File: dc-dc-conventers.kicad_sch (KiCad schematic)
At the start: 114 parts, among them Q13 DTC014TEBTL, Q14 DTC014TEBTL, Q15 DTC014TEBTL, Q18 DTC014TEBTL, U47 RT6236AHGQUF, U48 RT6236AHGQUF, U49 AP62301WU-7, U50 AP62301WU-7, U51 AP62301WU-7, U52 AP62301WU-7, U53 AP62301WU-7, U54 AP62301WU-7, U55 AP62301WU-7

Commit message: Added cosmetic changes to schematics (e.g. position of labels, designators)
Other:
- moved on the sheet: C184, C185, C186, C187, C188, C189, C190, C191, C192, C193, C194, C195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

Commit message: Fixed footprints
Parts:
- U47, U48: footprint kria-k26-devboard-footprints:RICHTEK_13-UFQFN -> antmicro-footprints:RT6236A
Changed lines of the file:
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@@
     (property "Reference" "U47" (id 0) (at 68.707 27.559 0))
     (property "Value" "RT6236AHGQUF" (id 1) (at 68.707 29.8704 0))
-    (property "Footprint" "kria-k26-devboard-footprints:RICHTEK_13-UFQFN" (id 2) (at 59.182 59.69 0)
+    (property "Footprint" "antmicro-footprints:RT6236A" (id 2) (at 59.182 59.69 0)
       (effects (font (size 1.27 1.27)) hide)
     )
@@
     (pin "2")
   )
-  (symbol (lib_id "kria-k26-devboard:RT6236AHGQUF") (at 68.834 100.838 0) (unit 1)
+  (symbol (lib_name "RT6236AHGQUF_1") (lib_id "kria-k26-devboard:RT6236AHGQUF") (at 68.834 100.838 0) (unit 1)
     (in_bom yes) (on_board yes)
     (property "Reference" "U48" (id 0) (at 68.199 81.407 0))
     (property "Value" "RT6236AHGQUF" (id 1) (at 68.199 83.7184 0))
-    (property "Footprint" "kria-k26-devboard-footprints:RICHTEK_13-UFQFN" (id 2) (at 58.674 113.538 0)
-      (effects (font (size 1.27 1.27)) hide)
-    )
+    (property "Footprint" "antmicro-footprints:RT6236A" (id 2) (at 58.674 113.538 0)
+      (effects (font (size 1.27 1.27)) hide)
+    )

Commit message: loclib
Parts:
- U47, U48: footprint antmicro-footprints:RT6236A -> kria-k26-devboard-footprints:RT6236A
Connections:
- net DC_MAIN_BUS: no longer U48.10 (VIN), U48.9 (VIN)
- net GND: no longer U48.1 (GND), U48.13 (GND)
- net SW_SOM_5V: no longer U48.12 (SW)
- net at C188.1: no longer U48.6 (PVCC)
- net at C190.1: no longer U48.5 (SS)
- net at C192.2: no longer U48.11 (BOOT)
- net at C194.1, R124.2, R125.1: no longer U48.3 (FB)
- net at R119.1: no longer U48.2 (EN)

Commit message: Replace 5V DC-DCs output capacitors to 16V rated ones
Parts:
- removed C195, C196, C197, C198, C199, C200: C_22u_0603, kria-k26-devboard-footprints:0603-cap, symbol kria-k26-devboard:C_22u_0603
- removed U48: RT6236AHGQUF, kria-k26-devboard-footprints:RT6236A, symbol kria-k26-devboard:RT6236AHGQUF
- added C195, C196, C197, C198, C199, C200: C_22u_0603_16V, antmicro-footprints:0603-cap, symbol antmicroCapacitors0603:C_22u_0603_16V
- added R156, R157, R158, R159, R160, R161, R162, R163, R164: R_0R_0603_HPWR, antmicro-footprints:0603-res, symbol antmicroResistors0603:R_0R_0603_HPWR
- added U48: RT6236AHGQUF, antmicro-footprints:RICHTEK_13-UFQFN, symbol antmicroPMICVoltageRegulatorsDCDCSwitchingRegulators:RT6236AHGQUF
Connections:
- net DC_MAIN_BUS: now also U48.10 (VIN), U48.9 (VIN); no longer C183.1, C185.1, R118.2, U47.10 (VIN), U47.9 (VIN)
- net GND: now also C196.2, C198.2, C200.2, U48.1 (GND), U48.13 (GND); no longer C183.2, C185.2, C187.2, C189.2, R123.2, U47.1 (GND), U47.13 (GND)
- net SOM_5V0: now also C196.1, C198.1, C200.1
- net SW_SOM_5V: now also U48.12 (SW)
- net USB_5V: now also C195.1, C197.1, C199.1
- net at C188.1: now also U48.6 (PVCC)
- net at C190.1: now also U48.5 (SS)
- net at C192.2: now also U48.11 (BOOT)
- net at C194.1, R124.2, R125.1: now also U48.3 (FB)
- net at R119.1: now also U48.2 (EN)
- new net: C183.2, C185.2, C187.2, C189.2, C195.2, C197.2, C199.2, R123.2, U47.1 (GND), U47.13 (GND)
- new net: C183.1, C185.1, R118.2, U47.10 (VIN), U47.9 (VIN)
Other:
- moved on the sheet: C183, C184, C185, C186, C187, C188, C189, C190, C191, C192, C193, C194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

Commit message: Add 0Ohm DC-DC output resistor WiP
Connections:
- net DC_MAIN_BUS: now also C183.1, C185.1, R118.2, U47.10 (VIN), U47.9 (VIN)
- net PL_1V2: now also R159.2; no longer C224.2, C226.2, L9.2 (P), R146.1, TP42.1
- net PL_3V3: now also R158.2; no longer C223.2, C225.2, L8.2 (P), R144.1, TP41.1
- net PS_1V0: now also R157.2; no longer C215.2, L7.2 (P), R139.1, TP40.1
- net PS_1V2: now also R156.2; no longer C214.2, C218.2, L6.2 (P), R137.1, TP39.1
- net PS_1V8: now also R164.2; no longer C213.2, C217.2, L5.2 (P), R135.1, TP38.1
- net PS_2V5: now also R163.2; no longer C212.2, L4.2 (P), R133.1, TP37.1
- net PS_3V3: now also R162.2; no longer C211.2, C216.2, L3.2 (P), R131.1, TP36.1
- net SOM_5V0: now also R161.2; no longer C194.2, C196.1, C198.1, C200.1, L2.2 (P), R124.1, TP50.1
- net USB_5V: now also R160.2; no longer C193.2, C195.1, C197.1, C199.1, L1.2 (P), R122.1, TP51.1
- net PS_1V2_OUT: now reaches R156.1
- net PS_1V2_OUT: now also C214.2, C218.2, L6.2 (P), R137.1, TP39.1
- net PS_1V8_OUT: now reaches R164.1
- net PS_1V8_OUT: now also C213.2, C217.2, L5.2 (P), R135.1, TP38.1
- net PS_3V3_OUT: now reaches R162.1
- net PS_3V3_OUT: now also C211.2, C216.2, L3.2 (P), R131.1, TP36.1
- net PS_1V0_OUT: now reaches R157.1
- net PS_1V0_OUT: now also C215.2, L7.2 (P), R139.1, TP40.1
- net PS_2V5_OUT: now reaches R163.1
- net PS_2V5_OUT: now also C212.2, L4.2 (P), R133.1, TP37.1
- net USB_5V_OUT: now reaches R160.1
- net USB_5V_OUT: now also C193.2, C195.1, C197.1, C199.1, L1.2 (P), R122.1, TP51.1
- net PL_3V3_OUT: now reaches R158.1
- net PL_3V3_OUT: now also C223.2, C225.2, L8.2 (P), R144.1, TP41.1
- net PL_1V2_OUT: now reaches R159.1
- net PL_1V2_OUT: now also C224.2, C226.2, L9.2 (P), R146.1, TP42.1
- net SOM_5V_OUT: now reaches R161.1
- net SOM_5V_OUT: now also C194.2, C196.1, C198.1, C200.1, L2.2 (P), R124.1, TP50.1
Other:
- moved on the sheet: C201, C202, C203, C204, C205, C206, C207, C208, C209, C210, C211, C212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

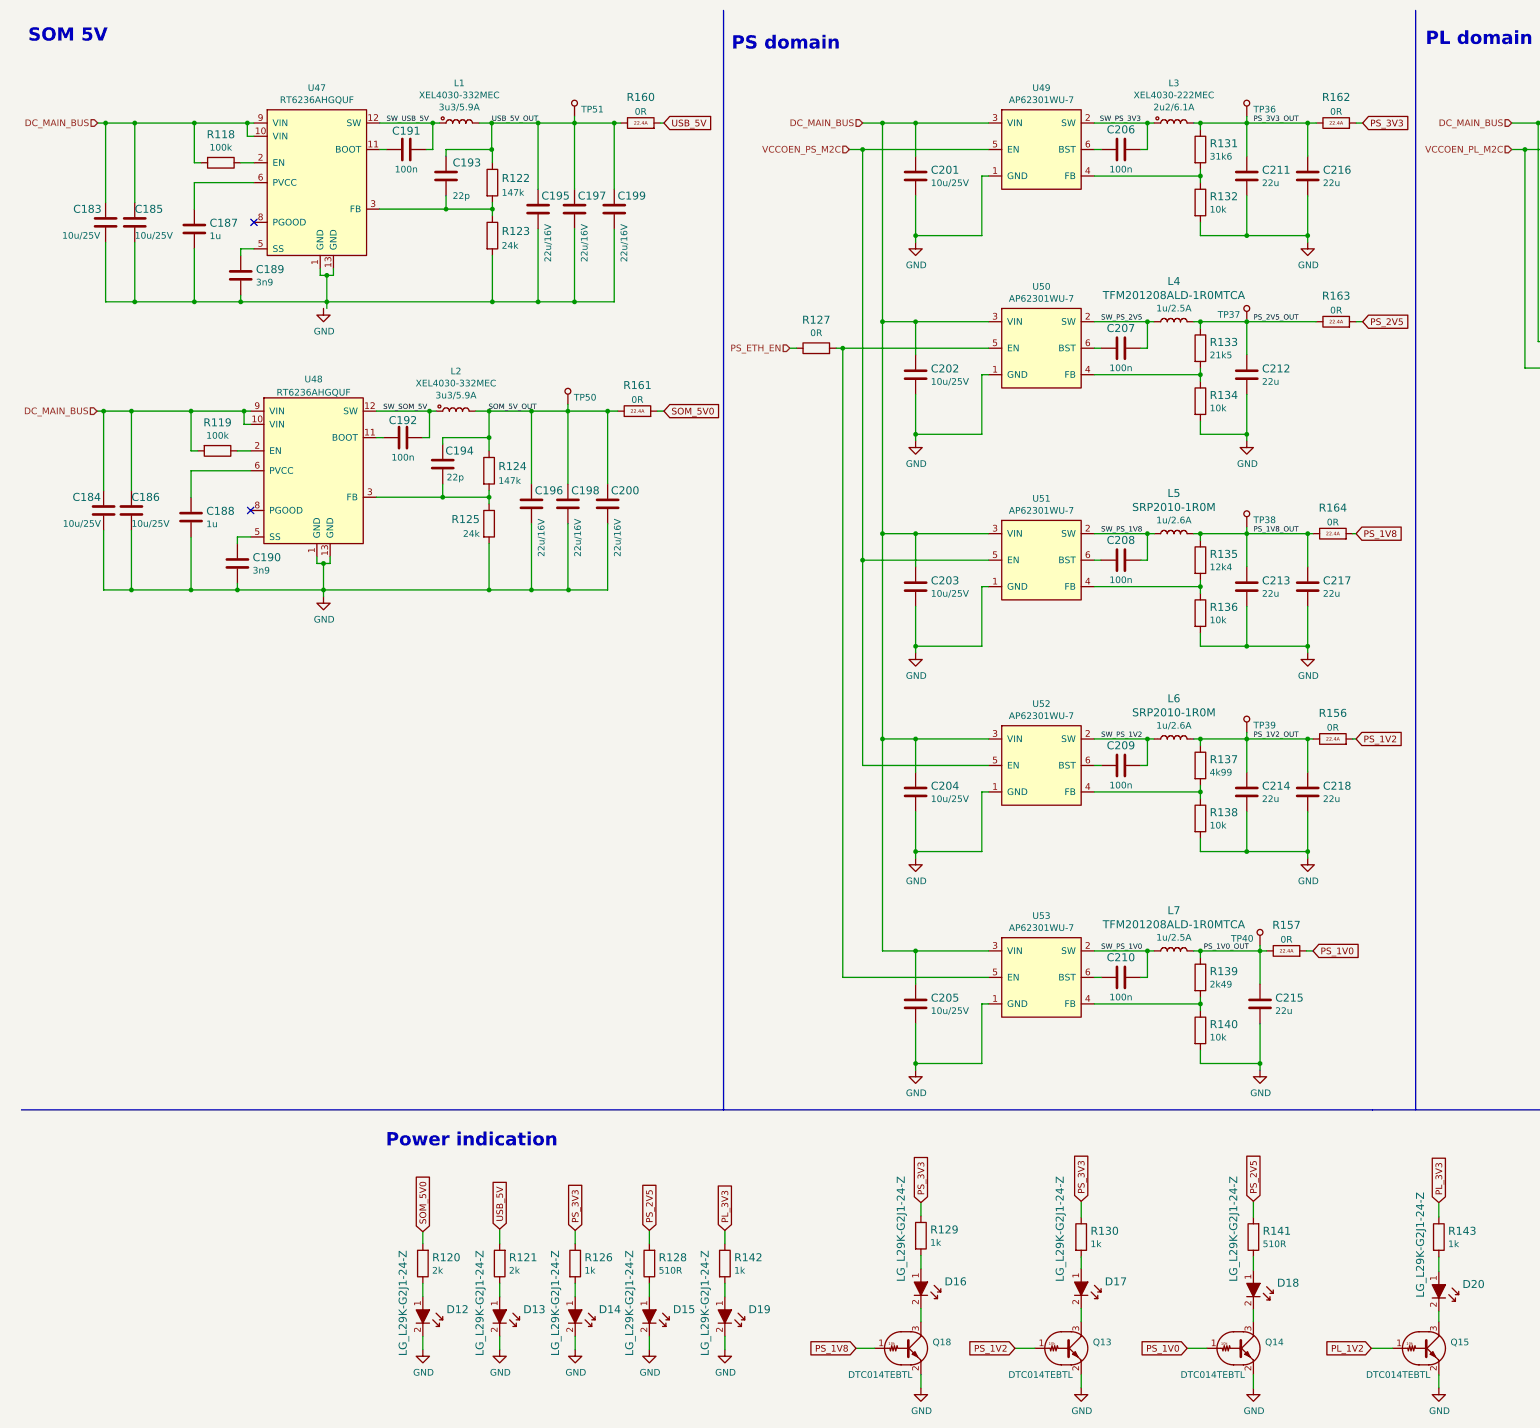
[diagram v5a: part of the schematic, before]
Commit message: Finish adding 0Ohm DC-DC output resistor
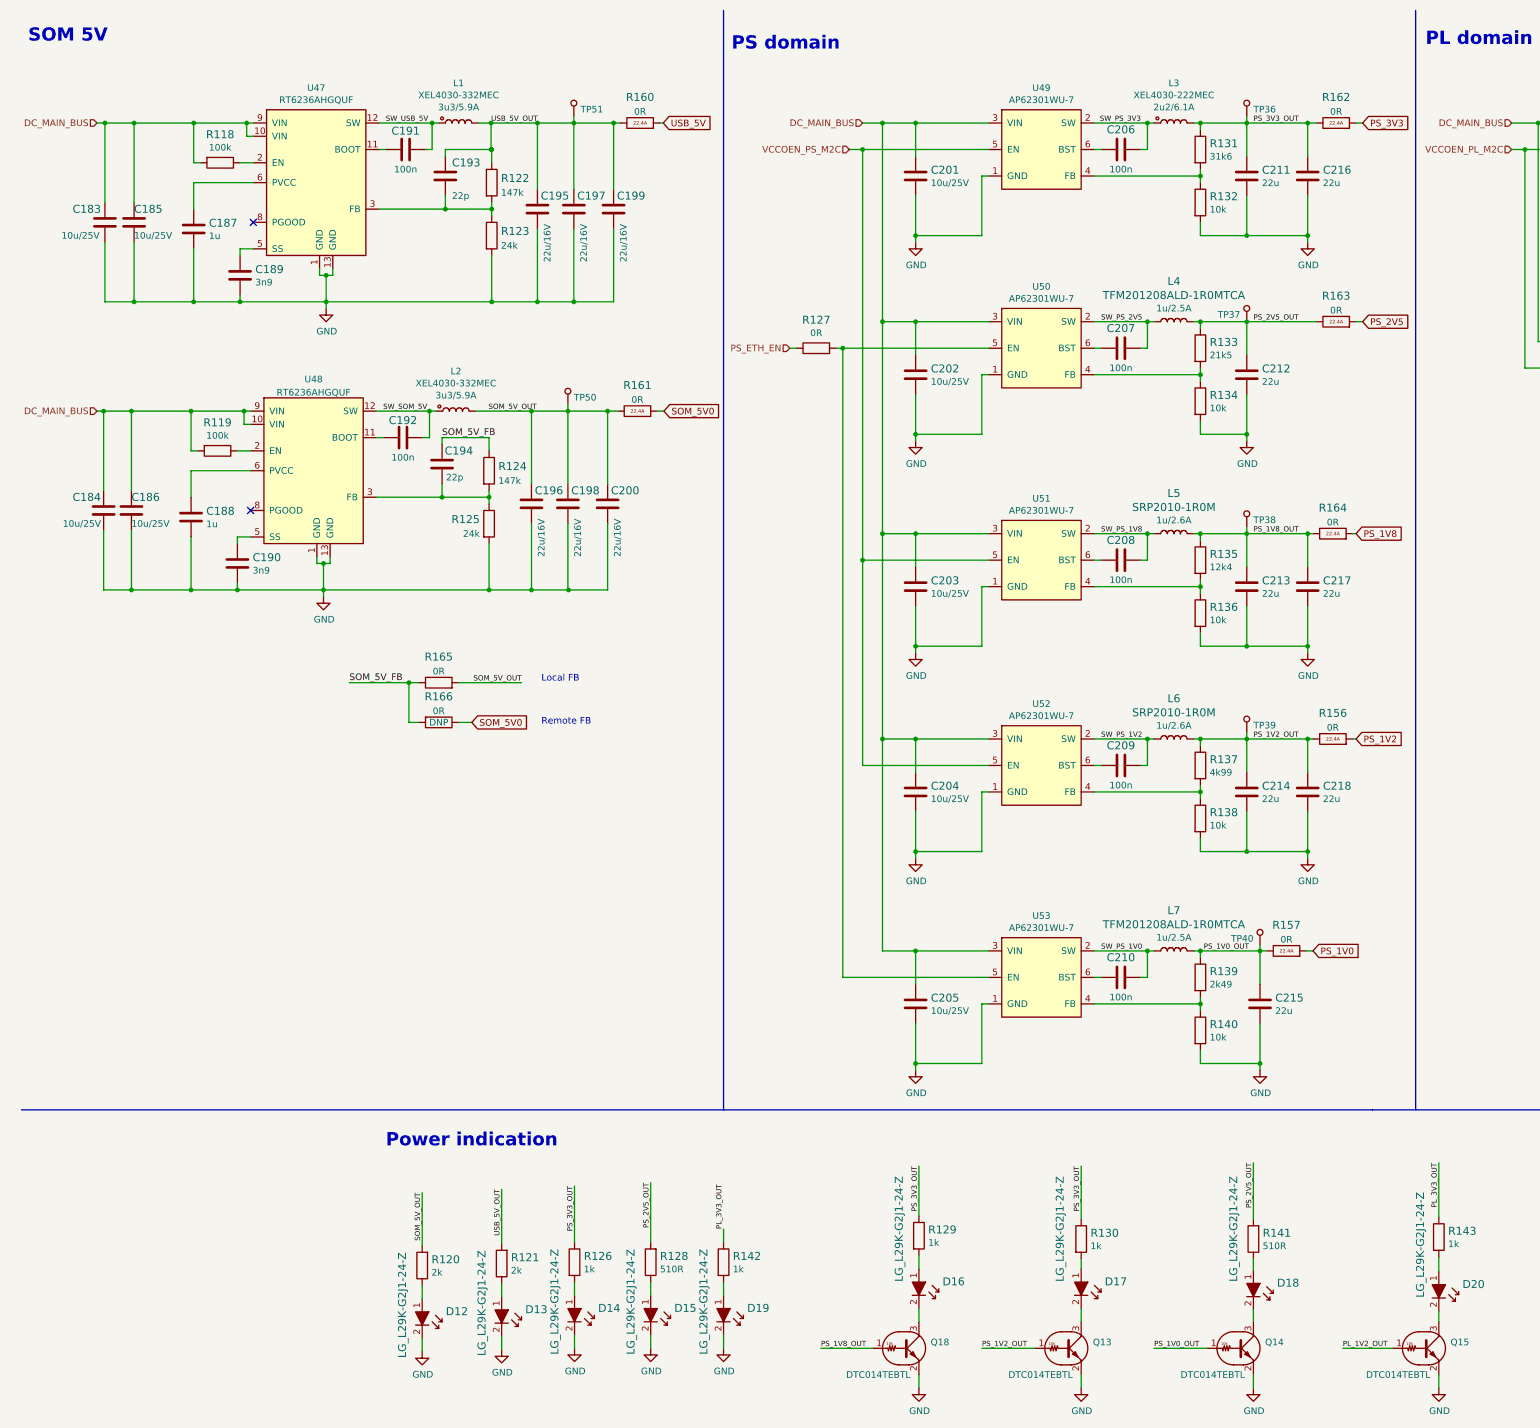
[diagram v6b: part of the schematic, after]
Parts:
- added R165, R166: R_0R_0402, antmicro-footprints:0402-res, symbol antmicroResistors0402:R_0R_0402
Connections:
- net GND: now also C183.2, C185.2, C187.2, C189.2, C195.2, C197.2, C199.2, R123.2, U47.1 (GND), U47.13 (GND)
- net PL_1V2: no longer Q15.1 (B)
- net PL_1V2_OUT: now also Q15.1 (B)
- net PL_3V3: no longer R142.1, R143.1
- net PL_3V3_OUT: now also R142.1, R143.1
- net PS_1V0: no longer Q14.1 (B)
- net PS_1V0_OUT: now also Q14.1 (B)
- net PS_1V2: no longer Q13.1 (B)
- net PS_1V2_OUT: now also Q13.1 (B)
- net PS_1V8: no longer Q18.1 (B)
- net PS_1V8_OUT: now also Q18.1 (B)
- net PS_2V5: no longer R128.2, R141.2
- net PS_2V5_OUT: now also R128.2, R141.2
- net PS_3V3: no longer R126.1, R129.1, R130.1
- net PS_3V3_OUT: now also R126.1, R129.1, R130.1
- net SOM_5V0: now also R166.1; no longer R120.2
- net SOM_5V_OUT: now also R120.2, R165.2; no longer C194.2, R124.1
- net USB_5V: no longer R121.2
- net USB_5V_OUT: now also R121.2
- new net SOM_5V_FB: C194.2, R124.1, R165.1, R166.2
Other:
- note added: "Local FB"
- note added: "Remote FB"

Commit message: Bump date and revision
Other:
- title: DC-DC converters -> Kria K26 Devboard
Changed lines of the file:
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@@
   (paper "A3")
   (title_block
-    (title "DC-DC converters")
-    (date "2022-07-25")
-    (rev "1.1.0")
+    (title "Kria K26 Devboard")
+    (date "2023-02-15")
+    (rev "1.1.1")
     (comment 1 "www.antmicro.com")
     (comment 2 "Antmicro Ltd.")

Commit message: Loclib of the project
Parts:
- C195, C196, C197, C198, C199, C200: footprint antmicro-footprints:0603-cap -> kria-k26-devboard-footprints:0603-cap; symbol antmicroCapacitors0603:C_22u_0603_16V -> kria-k26-devboard:C_22u_0603_16V
- R156, R157, R158, R159, R160, R161, R162, R163, R164: footprint antmicro-footprints:0603-res -> kria-k26-devboard-footprints:0603-res; symbol antmicroResistors0603:R_0R_0603_HPWR -> kria-k26-devboard:R_0R_0603_HPWR
- R165, R166: footprint antmicro-footprints:0402-res -> kria-k26-devboard-footprints:0402-res; symbol antmicroResistors0402:R_0R_0402 -> kria-k26-devboard:R_0R_0402
- U48: footprint antmicro-footprints:RICHTEK_13-UFQFN -> kria-k26-devboard-footprints:RICHTEK_13-UFQFN; symbol antmicroPMICVoltageRegulatorsDCDCSwitchingRegulators:RT6236AHGQUF -> kria-k26-devboard:RT6236AHGQUF
